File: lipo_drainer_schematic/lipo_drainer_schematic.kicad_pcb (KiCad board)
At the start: 2 copper layers, 122.5 x 88 mm, 62 parts, among them J1 BATT, J2 FAN, J3 Vcal, J4 128x64_OLED, J5 Gcal, J6 Ical, J7 Heatsink Temp (for MCP7901), Q1 MMBT3904, Q10 G700P06T, Q11 G700P06T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

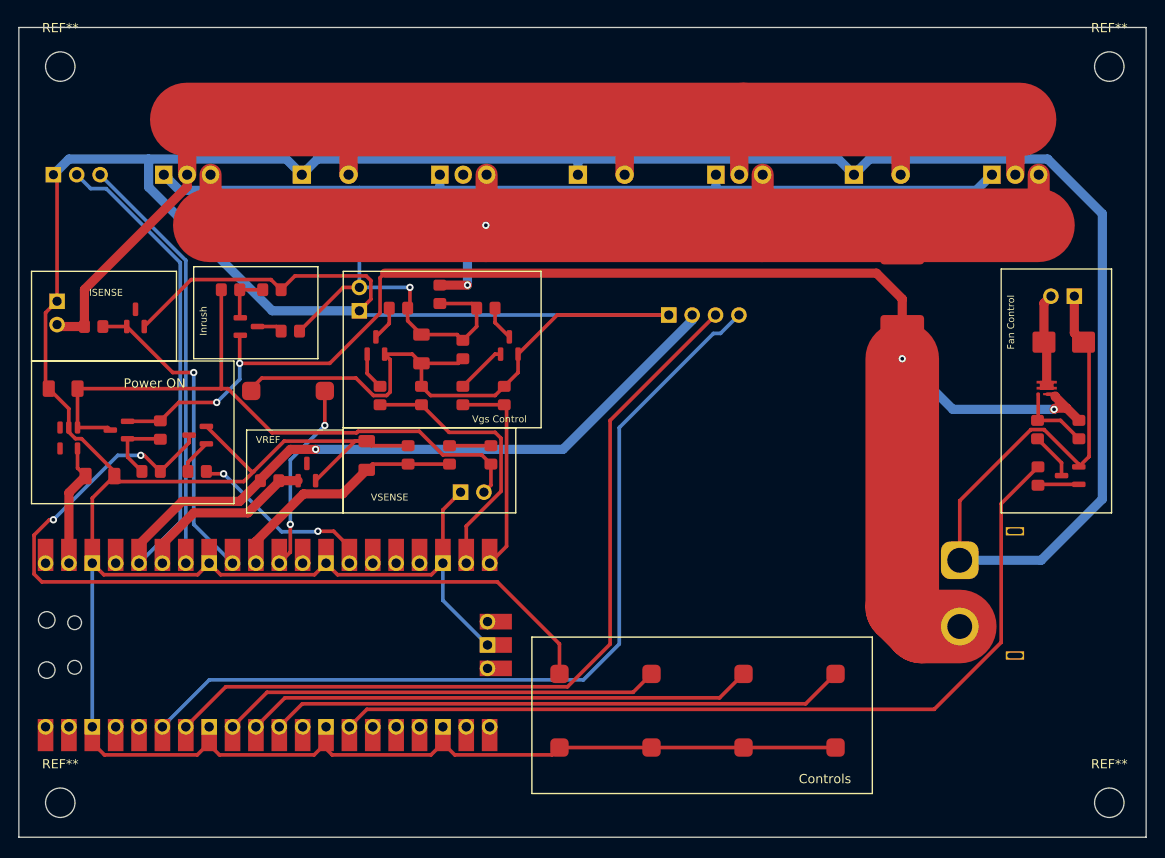
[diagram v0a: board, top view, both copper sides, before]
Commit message: added filled zones
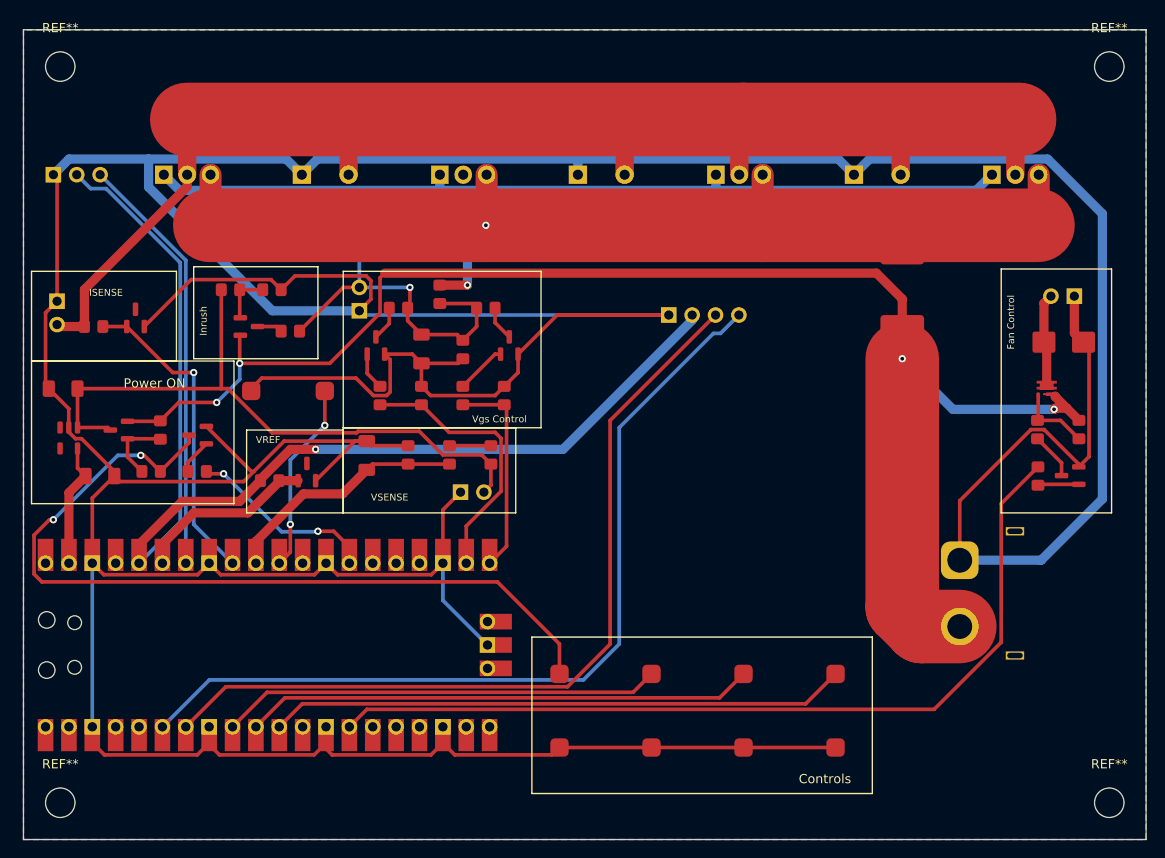
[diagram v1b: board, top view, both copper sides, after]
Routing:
- added copper zone on B.Cu, net GND
- added copper zone on F.Cu, net GND
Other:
- board size 122.5 x 88 mm -> 122 x 88 mm
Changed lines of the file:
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@@
   (gr_rect (start 106.5 75.75) (end 120 85.75)
     (stroke (width 0.15) (type default)) (fill none) (layer "F.SilkS"))
-  (gr_rect (start 87.5 49.75) (end 210 137.75)
+  (gr_rect (start 88 50) (end 210 138)
     (stroke (width 0.1) (type default)) (fill none) (layer "Edge.Cuts"))
   (gr_text "ISENSE" (at 95.125 79) (layer "F.SilkS")
@@
   (segment (start 105.64 75.06) (end 96.33 65.75) (width 0.4) (layer "B.Cu") (net 52))
   (segment (start 105.64 107.97) (end 105.64 75.06) (width 0.4) (layer "B.Cu") (net 52))
+  (zone (net 18) (net_name "GND") (layers "F&B.Cu") (hatch edge 0.5)
+    (connect_pads (clearance 0.5))
+    (min_thickness 0.25) (filled_areas_thickness no)
+    (fill yes (thermal_gap 0.5) (thermal_bridge_width 0.5))
+    (polygon
+      (pts
+        (xy 88 138)
+        (xy 210 138)
+        (xy 210 50)
+        (xy 88 50)
+      )
+    )
+  )
 )

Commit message: Label cleanup
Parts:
- J6: value Ical -> ICAL
- J7: value Heatsink Temp (for MCP7901) -> MCP7901; footprint Connector_PinHeader_2.54mm:PinHeader_1x03_P2.54mm_Vertical -> Package_TO_SOT_THT:TO-92_Inline
- moved J7 3.03 mm to (94.3, 66.0), turned to 180 degrees
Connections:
- J7 pad 1: GND -> /3V3
- J7 pad 2: /3V3 -> /TEMP
- J7 pad 3: /TEMP -> GND
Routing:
- net /TEMP: track 46.1 -> 50.2 mm, vias 0 -> 1
- net /3V3: track 124.4 -> 123.8 mm
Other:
- board text added: "CONTROLS"
- board text added: "FAN CONTROL"
- board text added: "INRUSH"
- board text added: "POWER ON"
- board text added: "Vgs CONTROL"
- board text removed: "Controls"
- board text removed: "Fan Control"
- board text removed: "Inrush"
- board text removed: "Power ON"
- board text removed: "Vgs Control"

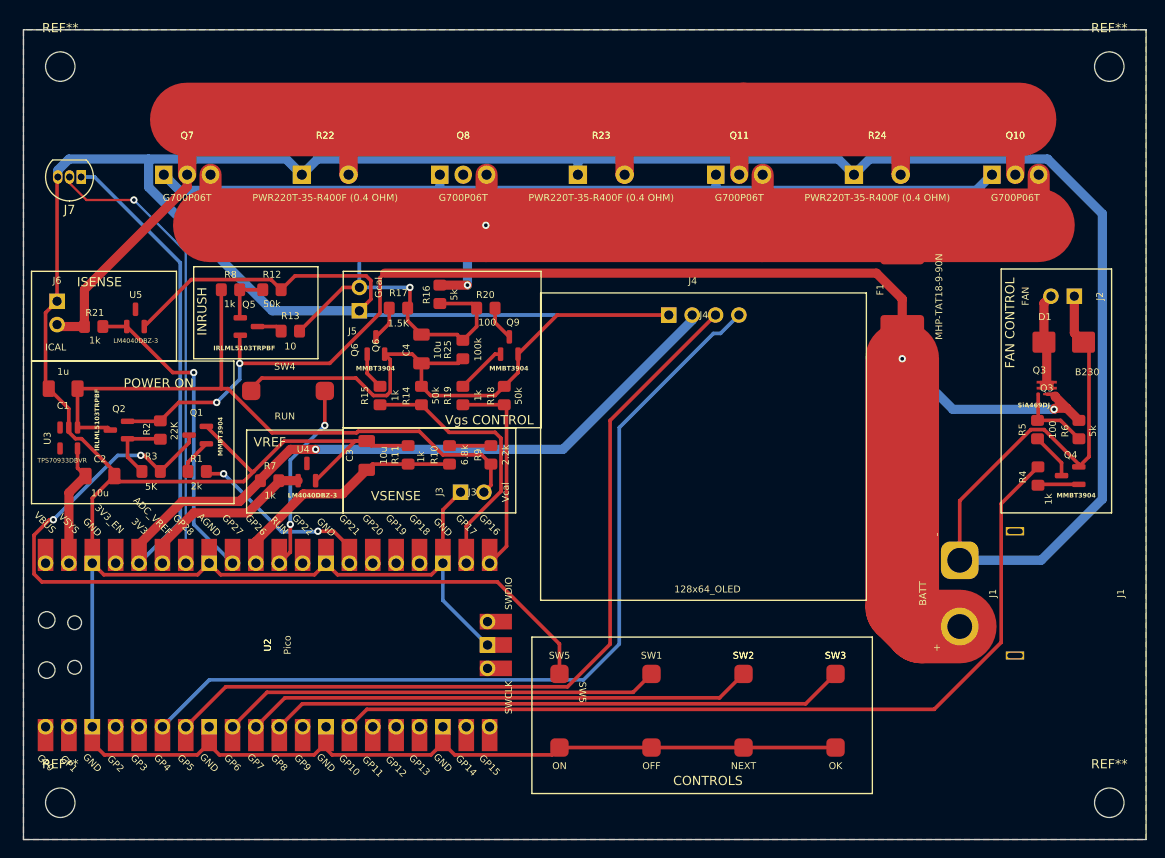
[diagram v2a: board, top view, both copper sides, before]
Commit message: Cleaned up almost all DRC warnings
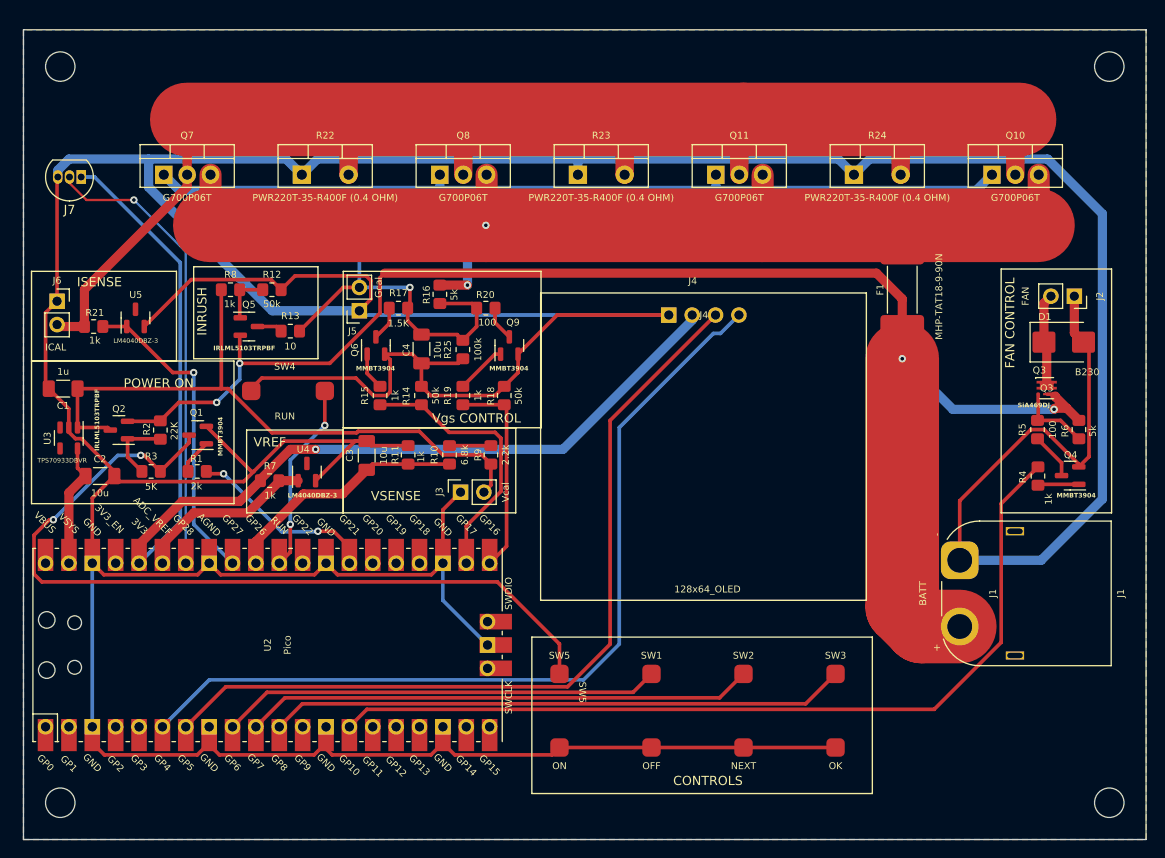
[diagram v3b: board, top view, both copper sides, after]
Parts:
- renumbered REF** to NEHOLE, REF** to NWHOLE, REF** to SEHOLE, REF** to SWHOLE
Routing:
- net /FET-D: track 211.4 -> 217.5 mm

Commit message: Added vias
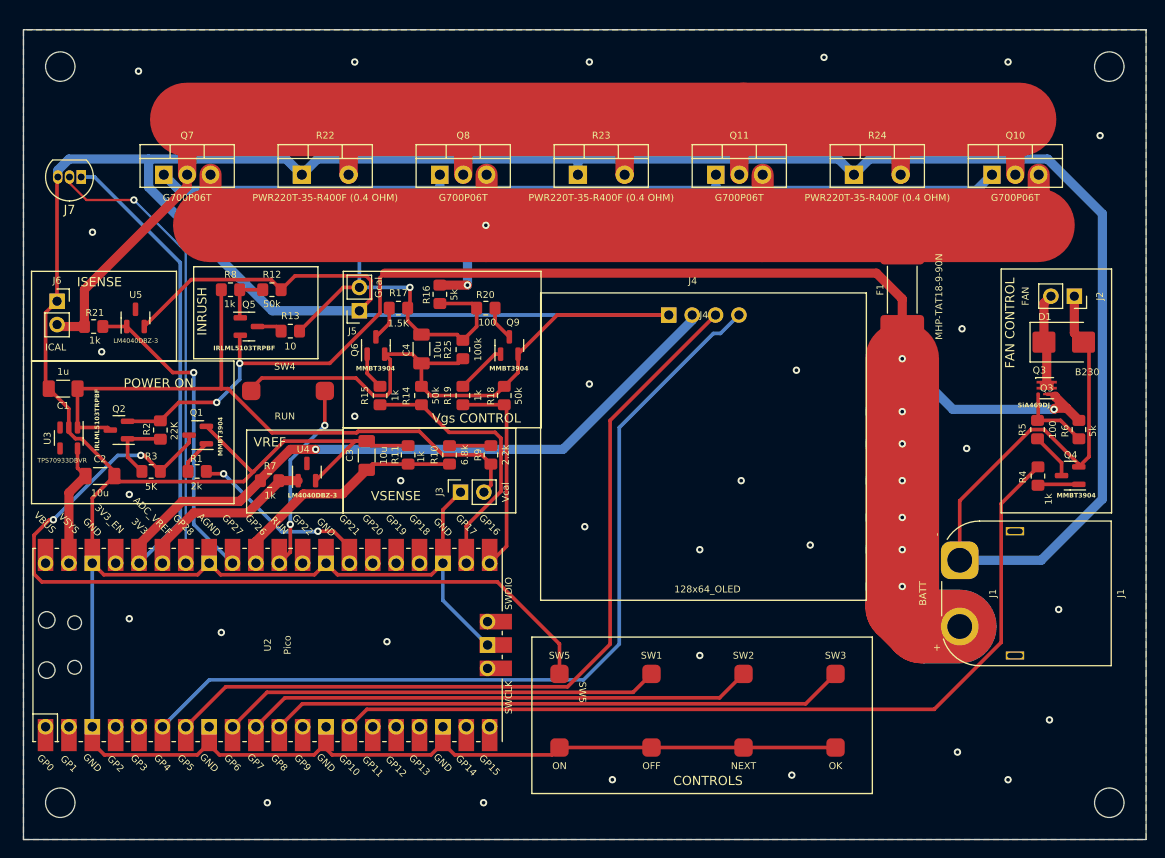
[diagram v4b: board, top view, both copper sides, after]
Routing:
- net /BAT+: track 160.6 -> 191.3 mm, vias 4 -> 10
- net GND: vias 0 -> 31
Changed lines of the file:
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@@
       (stroke (width 0.1) (type solid)) (layer "F.Fab"))
     (pad "1" thru_hole rect (at 0 0) (size 2 2) (drill 1.1) (layers "*.Cu" "*.Mask")
-      (net 18 "GND") (pintype "passive"))
+      (net 18 "GND") (pintype "passive") (thermal_bridge_width 20) (thermal_bridge_angle 45))
     (pad "2" thru_hole oval (at 5.08 0) (size 2 2) (drill 1.1) (layers "*.Cu" "*.Mask")
       (net 27 "/FET-D") (pintype "passive"))
@@
       (stroke (width 0.1) (type solid)) (layer "F.Fab"))
     (pad "1" thru_hole rect (at 0 0) (size 2 2) (drill 1.1) (layers "*.Cu" "*.Mask")
-      (net 18 "GND") (pintype "passive"))
+      (net 18 "GND") (pintype "passive") (thermal_bridge_width 20) (thermal_bridge_angle 45))
     (pad "2" thru_hole oval (at 5.08 0) (size 2 2) (drill 1.1) (layers "*.Cu" "*.Mask")
       (net 27 "/FET-D") (pintype "passive"))
@@
     (pad "" thru_hole rect (at 10.35 -6 270) (size 0.9 2) (drill oval 0.6 1.7) (layers "*.Cu" "*.Mask"))
     (pad "1" thru_hole roundrect (at 0 0 270) (size 4.1 4.1) (drill 2.7) (layers "*.Cu" "*.Mask") (roundrect_rratio 0.25)
-      (net 18 "GND") (pinfunction "Pin_1") (pintype "passive"))
+      (net 18 "GND") (pinfunction "Pin_1") (pintype "passive") (thermal_bridge_width 10) (thermal_bridge_angle 45))
     (pad "2" thru_hole circle (at 7.2 0 270) (size 4.1 4.1) (drill 2.7) (layers "*.Cu" "*.Mask")
-      (net 9 "/BAT+") (pinfunction "Pin_2") (pintype "passive"))
+      (net 9 "/BAT+") (pinfunction "Pin_2") (pintype "passive") (thermal_bridge_width 10))
     (model "${KICAD6_3DMODEL_DIR}/Connector_AMASS.3dshapes/AMASS_XT60PW-M_1x02_P7.20mm_Horizontal.wrl"
       (offset (xyz 0 0 0))
@@
       (stroke (width 0.1) (type solid)) (layer "F.Fab"))
     (pad "1" thru_hole rect (at 0 0) (size 2 2) (drill 1.1) (layers "*.Cu" "*.Mask")
-      (net 18 "GND") (pintype "passive"))
+      (net 18 "GND") (pintype "passive") (thermal_bridge_width 20) (thermal_bridge_angle 45))
     (pad "2" thru_hole oval (at 5.08 0) (size 2 2) (drill 1.1) (layers "*.Cu" "*.Mask")
       (net 27 "/FET-D") (pintype "passive"))
@@
       (net 27 "/FET-D") (pinfunction "D") (pintype "passive"))
     (pad "3" thru_hole oval (at 5.08 0) (size 1.905 2) (drill 1.1) (layers "*.Cu" "*.Mask")
-      (net 22 "/FET-S") (pinfunction "S") (pintype "passive"))
+      (net 22 "/FET-S") (pinfunction "S") (pintype "passive") (thermal_bridge_width 10) (thermal_bridge_angle 45))
     (model "${KICAD6_3DMODEL_DIR}/Package_TO_SOT_THT.3dshapes/TO-220-3_Vertical.wrl"
       (offset (xyz 0 0 0))
@@
   (segment (start 202.7 92.45) (end 201.375 91.125) (width 1) (layer "F.Cu") (net 9))
   (via (at 200 91.25) (size 0.8) (drill 0.4) (layers "F.Cu" "B.Cu") (net 9))
+  (via (at 183.5 99) (size 0.8) (drill 0.4) (layers "F.Cu" "B.Cu") (net 9))
+  (via (at 183.5 106.5) (size 0.8) (drill 0.4) (layers "F.Cu" "B.Cu") (net 9))
   (via (at 183.5 85.75) (size 0.8) (drill 0.4) (layers "F.Cu" "B.Cu") (net 9))
+  (via (at 183.5 91.5) (size 0.8) (drill 0.4) (layers "F.Cu" "B.Cu") (net 9))
+  (via (at 183.5 95) (size 0.8) (drill 0.4) (layers "F.Cu" "B.Cu") (net 9))
+  (via (at 183.5 103) (size 0.8) (drill 0.4) (layers "F.Cu" "B.Cu") (net 9))
+  (via (at 183.5 110.5) (size 0.8) (drill 0.4) (layers "F.Cu" "B.Cu") (net 9))
   (via (at 109 90.5) (size 0.8) (drill 0.4) (layers "F.Cu" "B.Cu") (net 9))
   (via (at 111.5 86.25) (size 0.8) (drill 0.4) (layers "F.Cu" "B.Cu") (net 9))
+  (segment (start 183.5 103) (end 183.5 99) (width 8) (layer "B.Cu") (net 9))
+  (segment (start 183.5 91.5) (end 183.5 89) (width 8) (layer "B.Cu") (net 9))
   (segment (start 189 91.25) (end 183.5 85.75) (width 1) (layer "B.Cu") (net 9))
+  (segment (start 185.85 114.85) (end 183.5 112.5) (width 8) (layer "B.Cu") (net 9))
+  (segment (start 183.5 99) (end 183.5 95) (width 8) (layer "B.Cu") (net 9))
+  (segment (start 189.75 114.85) (end 185.85 114.85) (width 8) (layer "B.Cu") (net 9))
+  (segment (start 183.5 106.5) (end 183.5 103) (width 8) (layer "B.Cu") (net 9))
   (segment (start 200 91.25) (end 189 91.25) (width 1) (layer "B.Cu") (net 9))
   (segment (start 111.5 88) (end 111.5 86.25) (width 0.4) (layer "B.Cu") (net 9))
   (segment (start 109 90.5) (end 111.5 88) (width 0.4) (layer "B.Cu") (net 9))
+  (segment (start 183.5 112.5) (end 183.5 110.5) (width 8) (layer "B.Cu") (net 9))
+  (segment (start 183.5 95) (end 183.5 91.5) (width 8) (layer "B.Cu") (net 9))
+  (segment (start 183.5 110.5) (end 183.5 106.5) (width 8) (layer "B.Cu") (net 9))
   (segment (start 198.275 92.375) (end 198.2 92.45) (width 0.4) (layer "F.Cu") (net 10))
   (segment (start 198.275 89.6) (end 198.275 92.375) (width 0.4) (layer "F.Cu") (net 10))
@@
   (segment (start 117.5 76.75) (end 116 78.25) (width 0.4) (layer "F.Cu") (net 18))
   (segment (start 203.8 96.3875) (end 203.8 84.55) (width 0.4) (layer "F.Cu") (net 18))
+  (via (at 114.5 134) (size 0.8) (drill 0.4) (layers "F.Cu" "B.Cu") (free) (net 18))
+  (via (at 172 87) (size 0.8) (drill 0.4) (layers "F.Cu" "B.Cu") (free) (net 18))
+  (via (at 127.5 116.5) (size 0.8) (drill 0.4) (layers "F.Cu" "B.Cu") (free) (net 18))
+  (via (at 96.5 85) (size 0.8) (drill 0.4) (layers "F.Cu" "B.Cu") (free) (net 18))
+  (via (at 199.5 125) (size 0.8) (drill 0.4) (layers "F.Cu" "B.Cu") (free) (net 18))
+  (via (at 152 131.5) (size 0.8) (drill 0.4) (layers "F.Cu" "B.Cu") (free) (net 18))
+  (via (at 124 53.5) (size 0.8) (drill 0.4) (layers "F.Cu" "B.Cu") (free) (net 18))
+  (via (at 109.5 115.5) (size 0.8) (drill 0.4) (layers "F.Cu" "B.Cu") (free) (net 18))
+  (via (at 161.5 106.5) (size 0.8) (drill 0.4) (layers "F.Cu" "B.Cu") (free) (net 18))
+  (via (at 100.5 54.5) (size 0.8) (drill 0.4) (layers "F.Cu" "B.Cu") (free) (net 18))
+  (via (at 195 53.5) (size 0.8) (drill 0.4) (layers "F.Cu" "B.Cu") (free) (net 18))
+  (via (at 171.5 131) (size 0.8) (drill 0.4) (layers "F.Cu" "B.Cu") (free) (net 18))
+  (via (at 129 99) (size 0.8) (drill 0.4) (layers "F.Cu" "B.Cu") (free) (net 18))
+  (via (at 161.5 118) (size 0.8) (drill 0.4) (layers "F.Cu" "B.Cu") (free) (net 18))
+  (via (at 175 53) (size 0.8) (drill 0.4) (layers "F.Cu" "B.Cu") (free) (net 18))
+  (via (at 200.5 113) (size 0.8) (drill 0.4) (layers "F.Cu" "B.Cu") (free) (net 18))
+  (via (at 124 92) (size 0.8) (drill 0.4) (layers "F.Cu" "B.Cu") (free) (net 18))
+  (via (at 99.5 114) (size 0.8) (drill 0.4) (layers "F.Cu" "B.Cu") (free) (net 18))
+  (via (at 195 131.5) (size 0.8) (drill 0.4) (layers "F.Cu" "B.Cu") (free) (net 18))
+  (via (at 190 82.5) (size 0.8) (drill 0.4) (layers "F.Cu" "B.Cu") (free) (net 18))
+  (via (at 189.5 128.5) (size 0.8) (drill 0.4) (layers "F.Cu" "B.Cu") (free) (net 18))
+  (via (at 190.5 95.5) (size 0.8) (drill 0.4) (layers "F.Cu" "B.Cu") (free) (net 18))
+  (via (at 205 61.5) (size 0.8) (drill 0.4) (layers "F.Cu" "B.Cu") (free) (net 18))
+  (via (at 95.5 72) (size 0.8) (drill 0.4) (layers "F.Cu" "B.Cu") (free) (net 18))
+  (via (at 166 99) (size 0.8) (drill 0.4) (layers "F.Cu" "B.Cu") (free) (net 18))
+  (via (at 149 104) (size 0.8) (drill 0.4) (layers "F.Cu" "B.Cu") (free) (net 18))
+  (via (at 149.5 88.5) (size 0.8) (drill 0.4) (layers "F.Cu" "B.Cu") (free) (net 18))
+  (via (at 138 134) (size 0.8) (drill 0.4) (layers "F.Cu" "B.Cu") (free) (net 18))
+  (via (at 149.5 53.5) (size 0.8) (drill 0.4) (layers "F.Cu" "B.Cu") (free) (net 18))
+  (via (at 99.5 100.5) (size 0.8) (drill 0.4) (layers "F.Cu" "B.Cu") (free) (net 18))
+  (via (at 173.5 106) (size 0.8) (drill 0.4) (layers "F.Cu" "B.Cu") (free) (net 18))
   (segment (start 199.3 64.05) (end 205.25 70) (width 1) (layer "B.Cu") (net 18))
   (segment (start 101.5975 64.05) (end 101.5975 67.0975) (width 1) (layer "B.Cu") (net 18))
@@
   (segment (start 165.79 60.21) (end 166.25 59.75) (width 2) (layer "F.Cu") (net 27))
   (segment (start 123.33 59.859424) (end 123.25 59.779424) (width 2) (layer "F.Cu") (net 27))
+  (segment (start 105.79 65.75) (end 105.79 59.79) (width 2) (layer "F.Cu") (net 27))
   (segment (start 94.625 82.25) (end 91.86 82.25) (width 1) (layer "F.Cu") (net 27))
   (segment (start 135.79 60.090021) (end 135.5 59.800021) (width 2) (layer "F.Cu") (net 27))
   (segment (start 123.33 65.75) (end 123.33 59.859424) (width 2) (layer "F.Cu") (net 27))
-  (segment (start 105.79 59.79) (end 105.75 59.75) (width 1) (layer "F.Cu") (net 27))
   (segment (start 165.79 65.75) (end 165.79 60.21) (width 2) (layer "F.Cu") (net 27))
   (segment (start 153.33 59.83) (end 153.33 65.75) (width 2) (layer "F.Cu") (net 27))
@@
   (segment (start 94.625 78.228196) (end 105.79 67.063196) (width 1) (layer "F.Cu") (net 27))
   (segment (start 94.625 82.25) (end 94.625 78.228196) (width 1) (layer "F.Cu") (net 27))
-  (segment (start 105.79 65.75) (end 105.79 59.79) (width 1) (layer "F.Cu") (net 27))
+  (segment (start 105.79 59.79) (end 105.75 59.75) (width 1) (layer "F.Cu") (net 27))
   (segment (start 183.33 59.83) (end 183.33 65.75) (width 2) (layer "F.Cu") (net 27))
   (segment (start 135.79 65.75) (end 135.79 60.090021) (width 2) (layer "F.Cu") (net 27))
